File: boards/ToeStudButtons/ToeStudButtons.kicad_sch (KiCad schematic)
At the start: 23 parts

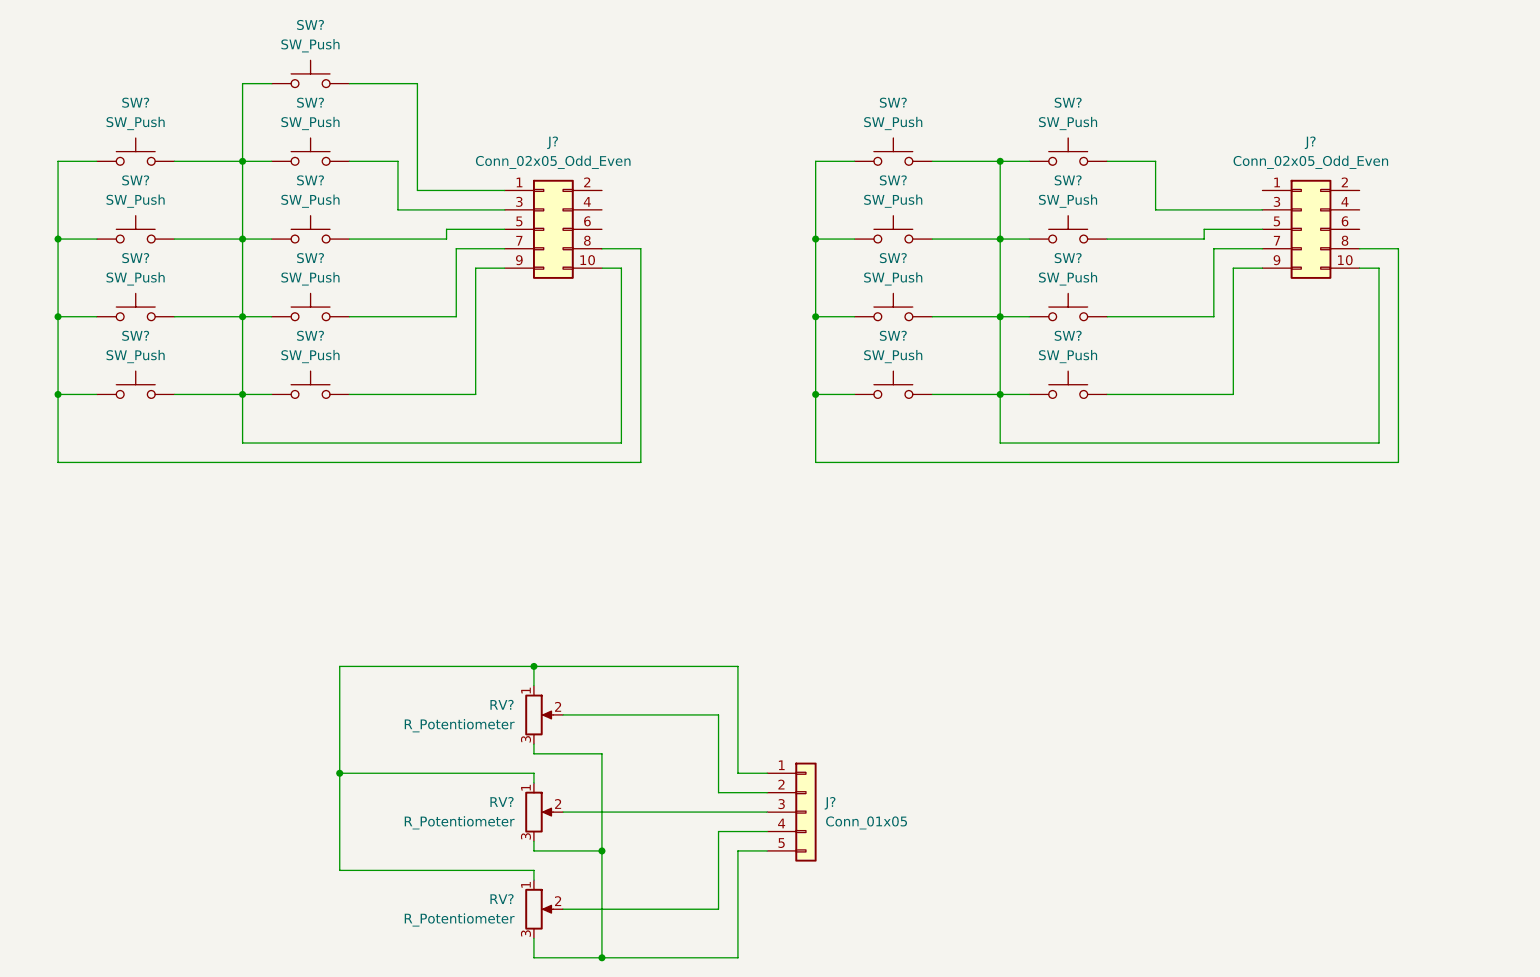
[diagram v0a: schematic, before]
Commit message: Renamed toestud encoder schematics
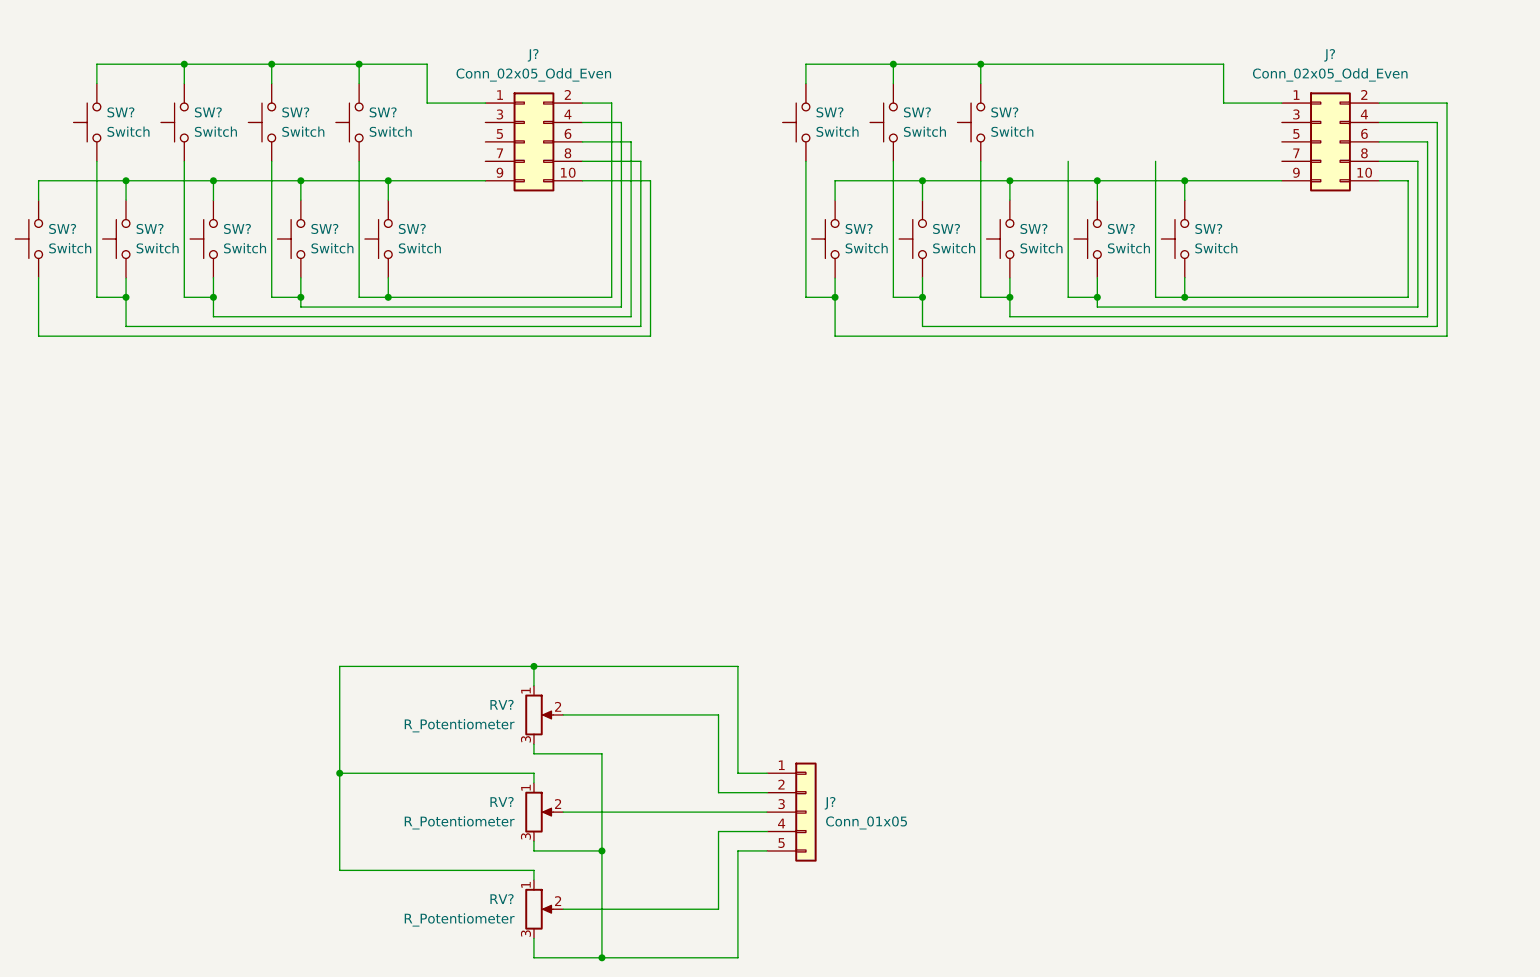
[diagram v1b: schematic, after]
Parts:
- removed J?: Conn_02x05_Odd_Even, symbol Connector_Generic:Conn_02x05_Odd_Even
- removed SW? (x16): SW_Push, symbol Switch:SW_Push
- added J?: Conn_02x05_Odd_Even, symbol Connector_Generic:Conn_02x05_Odd_Even
- added SW? (x16): Switch, symbol Switch:SW_Push
- SW?: value SW_Push -> Switch
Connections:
- net at J?.10 (Pin_10): now also SW?.1; no longer SW?.2
- net at J?.9 (Pin_9): now also SW?.2, SW?.2, SW?.2, SW?.2, SW?.2
- net at J?.1 (Pin_1): now also SW?.2, SW?.2, SW?.2, SW?.2
- net at SW?.1: now also J?.6 (Pin_6), SW?.1; no longer J?.8 (Pin_8)
- net at J?.2 (Pin_2): now also SW?.1, SW?.1
- net at J?.4 (Pin_4): now also SW?.1, SW?.1
- new net: J?.2 (Pin_2), SW?.1, SW?.1
- new net: J?.9 (Pin_9), SW?.2, SW?.2, SW?.2, SW?.2, SW?.2
- new net: J?.4 (Pin_4), SW?.1, SW?.1
- new net: J?.1 (Pin_1), SW?.2, SW?.2, SW?.2
- new net: J?.10 (Pin_10), SW?.1
- new net: J?.8 (Pin_8), SW?.1, SW?.1
- new net: J?.8 (Pin_8), SW?.1
- new net: J?.6 (Pin_6), SW?.1, SW?.1
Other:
- moved on the sheet: J?, SW?

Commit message: Renamed toe stud connectors
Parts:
- J?: value Conn_01x05 -> Swell
- J?: value Conn_02x05_Odd_Even -> ToeLeft
- J?: value Conn_02x05_Odd_Even -> ToeRight
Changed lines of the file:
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@@
       (effects (font (size 1.27 1.27)) (justify left))
     )
-    (property "Value" "Conn_01x05" (id 1) (at 132.08 151.1299 0)
+    (property "Value" "Swell" (id 1) (at 132.08 151.1299 0)
       (effects (font (size 1.27 1.27)) (justify left))
     )
@@
     (in_bom yes) (on_board yes) (fields_autoplaced)
     (property "Reference" "J?" (id 0) (at 93.98 50.8 0))
-    (property "Value" "Conn_02x05_Odd_Even" (id 1) (at 93.98 53.34 0))
+    (property "Value" "ToeLeft" (id 1) (at 93.98 53.34 0))
     (property "Footprint" "" (id 2) (at 92.71 62.23 0)
       (effects (font (size 1.27 1.27)) hide)
@@
     (in_bom yes) (on_board yes) (fields_autoplaced)
     (property "Reference" "J?" (id 0) (at 198.12 50.8 0))
-    (property "Value" "Conn_02x05_Odd_Even" (id 1) (at 198.12 53.34 0))
+    (property "Value" "ToeRight" (id 1) (at 198.12 53.34 0))
     (property "Footprint" "" (id 2) (at 196.85 62.23 0)
       (effects (font (size 1.27 1.27)) hide)
@@
   (symbol_instances
     (path "/013ddb12-11ad-42dd-961e-e451a0ddec44"
-      (reference "J?") (unit 1) (value "Conn_01x05") (footprint "")
+      (reference "J?") (unit 1) (value "Swell") (footprint "")
     )
     (path "/cdbdaf5a-4f5c-4def-9199-0945d415bcc6"
-      (reference "J?") (unit 1) (value "Conn_02x05_Odd_Even") (footprint "")
+      (reference "J?") (unit 1) (value "ToeLeft") (footprint "")
     )
     (path "/e5668fd5-5c1a-4135-9c84-197ad8913ff5"
-      (reference "J?") (unit 1) (value "Conn_02x05_Odd_Even") (footprint "")
+      (reference "J?") (unit 1) (value "ToeRight") (footprint "")
     )
     (path "/31bcb6f9-89ee-4aae-8ffe-ddc6900c2917"

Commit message: Updated Pedal Encoder to use UART from ToeStudEncoder
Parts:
- added J?: MIDI Out, symbol Connector:DIN-5_180degree
- added J?: MIDI In, symbol Connector:DIN-5_180degree
- added J?: MIDI In, symbol Connector_Generic:Conn_01x03
- added J?: MIDI Out, symbol Connector_Generic:Conn_01x03
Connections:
- new net: J?.2, J?.3 (Pin_3) (x2)
- new net: J?.1 (Pin_1), J?.4 (x2)
- new net: J?.2 (Pin_2), J?.5 (x2)
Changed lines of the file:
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@@
   (junction (at 140.97 52.07) (diameter 0) (color 0 0 0 0)
   )
+  (wire (pts (xy 199.39 138.43) (xy 199.39 124.46))
+    (stroke (width 0) (type default) (color 0 0 0 0))
+  )
   (wire (pts (xy 48.26 52.07) (xy 48.26 54.61))
     (stroke (width 0) (type default) (color 0 0 0 0))
@@
     (stroke (width 0) (type default) (color 0 0 0 0))
   )
+  (wire (pts (xy 193.04 118.11) (xy 199.39 118.11))
+    (stroke (width 0) (type default) (color 0 0 0 0))
+  )
   (wire (pts (xy 52.07 82.55) (xy 52.07 80.01))
     (stroke (width 0) (type default) (color 0 0 0 0))
@@
     (stroke (width 0) (type default) (color 0 0 0 0))
   )
+  (wire (pts (xy 223.52 115.57) (xy 219.71 115.57))
+    (stroke (width 0) (type default) (color 0 0 0 0))
+  )
   (wire (pts (xy 48.26 64.77) (xy 48.26 82.55))
     (stroke (width 0) (type default) (color 0 0 0 0))
@@
     (stroke (width 0) (type default) (color 0 0 0 0))
   )
+  (wire (pts (xy 212.09 147.32) (xy 212.09 146.05))
+    (stroke (width 0) (type default) (color 0 0 0 0))
+  )
   (wire (pts (xy 156.21 67.31) (xy 156.21 69.85))
     (stroke (width 0) (type default) (color 0 0 0 0))
@@
     (stroke (width 0) (type default) (color 0 0 0 0))
   )
+  (wire (pts (xy 199.39 147.32) (xy 212.09 147.32))
+    (stroke (width 0) (type default) (color 0 0 0 0))
+  )
   (wire (pts (xy 68.58 144.78) (xy 68.58 157.48))
     (stroke (width 0) (type default) (color 0 0 0 0))
@@
     (stroke (width 0) (type default) (color 0 0 0 0))
   )
+  (wire (pts (xy 193.04 140.97) (xy 204.47 140.97))
+    (stroke (width 0) (type default) (color 0 0 0 0))
+  )
   (wire (pts (xy 129.54 54.61) (xy 129.54 52.07))
     (stroke (width 0) (type default) (color 0 0 0 0))
@@
     (stroke (width 0) (type default) (color 0 0 0 0))
   )
+  (wire (pts (xy 199.39 113.03) (xy 199.39 99.06))
+    (stroke (width 0) (type default) (color 0 0 0 0))
+  )
   (wire (pts (xy 106.68 62.23) (xy 106.68 85.09))
     (stroke (width 0) (type default) (color 0 0 0 0))
@@
     (stroke (width 0) (type default) (color 0 0 0 0))
   )
+  (wire (pts (xy 223.52 124.46) (xy 223.52 140.97))
+    (stroke (width 0) (type default) (color 0 0 0 0))
+  )
   (wire (pts (xy 175.26 64.77) (xy 175.26 82.55))
     (stroke (width 0) (type default) (color 0 0 0 0))
@@
     (stroke (width 0) (type default) (color 0 0 0 0))
   )
+  (wire (pts (xy 193.04 138.43) (xy 199.39 138.43))
+    (stroke (width 0) (type default) (color 0 0 0 0))
+  )
+  (wire (pts (xy 193.04 115.57) (xy 204.47 115.57))
+    (stroke (width 0) (type default) (color 0 0 0 0))
+  )
   (wire (pts (xy 100.33 67.31) (xy 109.22 67.31))
     (stroke (width 0) (type default) (color 0 0 0 0))
@@
     (stroke (width 0) (type default) (color 0 0 0 0))
   )
+  (wire (pts (xy 199.39 143.51) (xy 199.39 147.32))
+    (stroke (width 0) (type default) (color 0 0 0 0))
+  )
   (wire (pts (xy 129.54 52.07) (xy 140.97 52.07))
     (stroke (width 0) (type default) (color 0 0 0 0))
@@
     (stroke (width 0) (type default) (color 0 0 0 0))
   )
+  (wire (pts (xy 193.04 143.51) (xy 199.39 143.51))
+    (stroke (width 0) (type default) (color 0 0 0 0))
+  )
+  (wire (pts (xy 199.39 124.46) (xy 223.52 124.46))
+    (stroke (width 0) (type default) (color 0 0 0 0))
+  )
   (wire (pts (xy 140.97 52.07) (xy 152.4 52.07))
     (stroke (width 0) (type default) (color 0 0 0 0))
@@
     (stroke (width 0) (type default) (color 0 0 0 0))
   )
+  (wire (pts (xy 212.09 121.92) (xy 212.09 120.65))
+    (stroke (width 0) (type default) (color 0 0 0 0))
+  )
   (wire (pts (xy 59.69 82.55) (xy 63.5 82.55))
     (stroke (width 0) (type default) (color 0 0 0 0))
@@
     (stroke (width 0) (type default) (color 0 0 0 0))
   )
+  (wire (pts (xy 199.39 118.11) (xy 199.39 121.92))
+    (stroke (width 0) (type default) (color 0 0 0 0))
+  )
   (wire (pts (xy 63.5 67.31) (xy 63.5 69.85))
     (stroke (width 0) (type default) (color 0 0 0 0))
@@
     (stroke (width 0) (type default) (color 0 0 0 0))
   )
+  (wire (pts (xy 199.39 99.06) (xy 223.52 99.06))
+    (stroke (width 0) (type default) (color 0 0 0 0))
+  )
   (wire (pts (xy 93.98 144.78) (xy 93.98 146.05))
     (stroke (width 0) (type default) (color 0 0 0 0))
@@
     (stroke (width 0) (type default) (color 0 0 0 0))
   )
+  (wire (pts (xy 223.52 99.06) (xy 223.52 115.57))
+    (stroke (width 0) (type default) (color 0 0 0 0))
+  )
   (wire (pts (xy 144.78 86.36) (xy 144.78 82.55))
     (stroke (width 0) (type default) (color 0 0 0 0))
@@
     (stroke (width 0) (type default) (color 0 0 0 0))
   )
+  (wire (pts (xy 193.04 113.03) (xy 199.39 113.03))
+    (stroke (width 0) (type default) (color 0 0 0 0))
+  )
   (wire (pts (xy 36.83 54.61) (xy 36.83 52.07))
     (stroke (width 0) (type default) (color 0 0 0 0))
@@
     (stroke (width 0) (type default) (color 0 0 0 0))
   )
+  (wire (pts (xy 199.39 121.92) (xy 212.09 121.92))
+    (stroke (width 0) (type default) (color 0 0 0 0))
+  )
   (wire (pts (xy 144.78 82.55) (xy 144.78 80.01))
+    (stroke (width 0) (type default) (color 0 0 0 0))
+  )
+  (wire (pts (xy 223.52 140.97) (xy 219.71 140.97))
     (stroke (width 0) (type default) (color 0 0 0 0))
   )
@@
     (pin "2")
   )
+  (symbol (lib_id "Connector:DIN-5_180degree") (at 212.09 138.43 180) (unit 1)
+    (in_bom yes) (on_board yes) (fields_autoplaced)
+    (property "Reference" "J?" (id 0) (at 212.0899 128.27 0))
+    (property "Value" "MIDI Out" (id 1) (at 212.0899 130.81 0))
+    (property "Footprint" "" (id 2) (at 212.09 138.43 0)
+      (effects (font (size 1.27 1.27)) hide)
+    )
+    (property "Datasheet" "http://www.mouser.com/ds/2/18/40_c091_abd_e-75918.pdf" (id 3) (at 212.09 138.43 0)
+      (effects (font (size 1.27 1.27)) hide)
+    )
+    (pin "1")
+    (pin "2")
+    (pin "3")
+    (pin "4")
+    (pin "5")
+  )
   (symbol (lib_id "Switch:SW_Push") (at 71.12 59.69 90) (unit 1)
     (in_bom yes) (on_board yes) (fields_autoplaced)
@@
     (pin "1")
     (pin "2")
+  )
+  (symbol (lib_id "Connector:DIN-5_180degree") (at 212.09 113.03 180) (unit 1)
+    (in_bom yes) (on_board yes) (fields_autoplaced)
+    (property "Reference" "J?" (id 0) (at 212.0899 102.87 0))
+    (property "Value" "MIDI In" (id 1) (at 212.0899 105.41 0))
+    (property "Footprint" "" (id 2) (at 212.09 113.03 0)
+      (effects (font (size 1.27 1.27)) hide)
+    )
+    (property "Datasheet" "http://www.mouser.com/ds/2/18/40_c091_abd_e-75918.pdf" (id 3) (at 212.09 113.03 0)
+      (effects (font (size 1.27 1.27)) hide)
+    )
+    (pin "1")
+    (pin "2")
+    (pin "3")
+    (pin "4")
+    (pin "5")
+  )
+  (symbol (lib_id "Connector_Generic:Conn_01x03") (at 187.96 115.57 0) (mirror y) (unit 1)
+    (in_bom yes) (on_board yes) (fields_autoplaced)
+    (property "Reference" "J?" (id 0) (at 187.96 106.68 0))
+    (property "Value" "MIDI In" (id 1) (at 187.96 109.22 0))
+    (property "Footprint" "" (id 2) (at 187.96 115.57 0)
+      (effects (font (size 1.27 1.27)) hide)
+    )
+    (property "Datasheet" "~" (id 3) (at 187.96 115.57 0)
+      (effects (font (size 1.27 1.27)) hide)
+    )
+    (pin "1")
+    (pin "2")
+    (pin "3")
   )
   (symbol (lib_id "Switch:SW_Push") (at 144.78 74.93 90) (unit 1)
@@
     (pin "2")
   )
+  (symbol (lib_id "Connector_Generic:Conn_01x03") (at 187.96 140.97 0) (mirror y) (unit 1)
+    (in_bom yes) (on_board yes) (fields_autoplaced)
+    (property "Reference" "J?" (id 0) (at 187.96 132.08 0))
+    (property "Value" "MIDI Out" (id 1) (at 187.96 134.62 0))
+    (property "Footprint" "" (id 2) (at 187.96 140.97 0)
+      (effects (font (size 1.27 1.27)) hide)
+    )
+    (property "Datasheet" "~" (id 3) (at 187.96 140.97 0)
+      (effects (font (size 1.27 1.27)) hide)
+    )
+    (pin "1")
+    (pin "2")
+    (pin "3")
+  )
   (symbol (lib_id "Switch:SW_Push") (at 63.5 74.93 90) (unit 1)
     (in_bom yes) (on_board yes)
@@
       (reference "J?") (unit 1) (value "Swell") (footprint "")
     )
+    (path "/7a66d561-c696-4436-97c6-12745c2aff4e"
+      (reference "J?") (unit 1) (value "MIDI Out") (footprint "")
+    )
+    (path "/b323ada5-d8f3-4c50-a580-78a26bc81aa9"
+      (reference "J?") (unit 1) (value "MIDI In") (footprint "")
+    )
+    (path "/b7545f27-7eff-425b-b150-2f803ce1c381"
+      (reference "J?") (unit 1) (value "MIDI In") (footprint "")
+    )
     (path "/cdbdaf5a-4f5c-4def-9199-0945d415bcc6"
       (reference "J?") (unit 1) (value "ToeLeft") (footprint "")
     )
+    (path "/d4ab6b65-4e24-4496-b9b8-e317f15d63e2"
+      (reference "J?") (unit 1) (value "MIDI Out") (footprint "")
+    )
     (path "/e5668fd5-5c1a-4135-9c84-197ad8913ff5"
